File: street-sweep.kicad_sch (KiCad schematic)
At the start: 56 parts, among them J1 PJ-320A, P1 GT-USB-7010ASV, SW10 SW_Push, SW10_r1 SW_Push, SW11 SW_Push, SW11_r1 SW_Push, SW12 SW_Push, SW12_r1 SW_Push, SW13_r1 SW_Push, SW14 SW_Push, SW14_r1 SW_Push, SW15 SW_Push, SW15_r1 SW_Push, SW16 SW_Push, SW16_r1 SW_Push, SW17 SW_Push, SW17_r1 SW_Push, SW18 SW_Push, SW18_r1 SW_Push, SW2 SW_Push, SW20 SW_Push, SW21 SW_Push, SW2_r1 SW_Push, SW3 SW_Push, SW3_r1 SW_Push, SW4 SW_Push, SW4_r1 SW_Push, SW5 SW_Push, SW5_r1 SW_Push, SW6 SW_Push, SW6_r1 SW_Push, SW7_r1 SW_Push, SW8 SW_Push, SW8_r1 SW_Push, SW9 SW_Push, SW9_r1 SW_Push, U1 CH552G

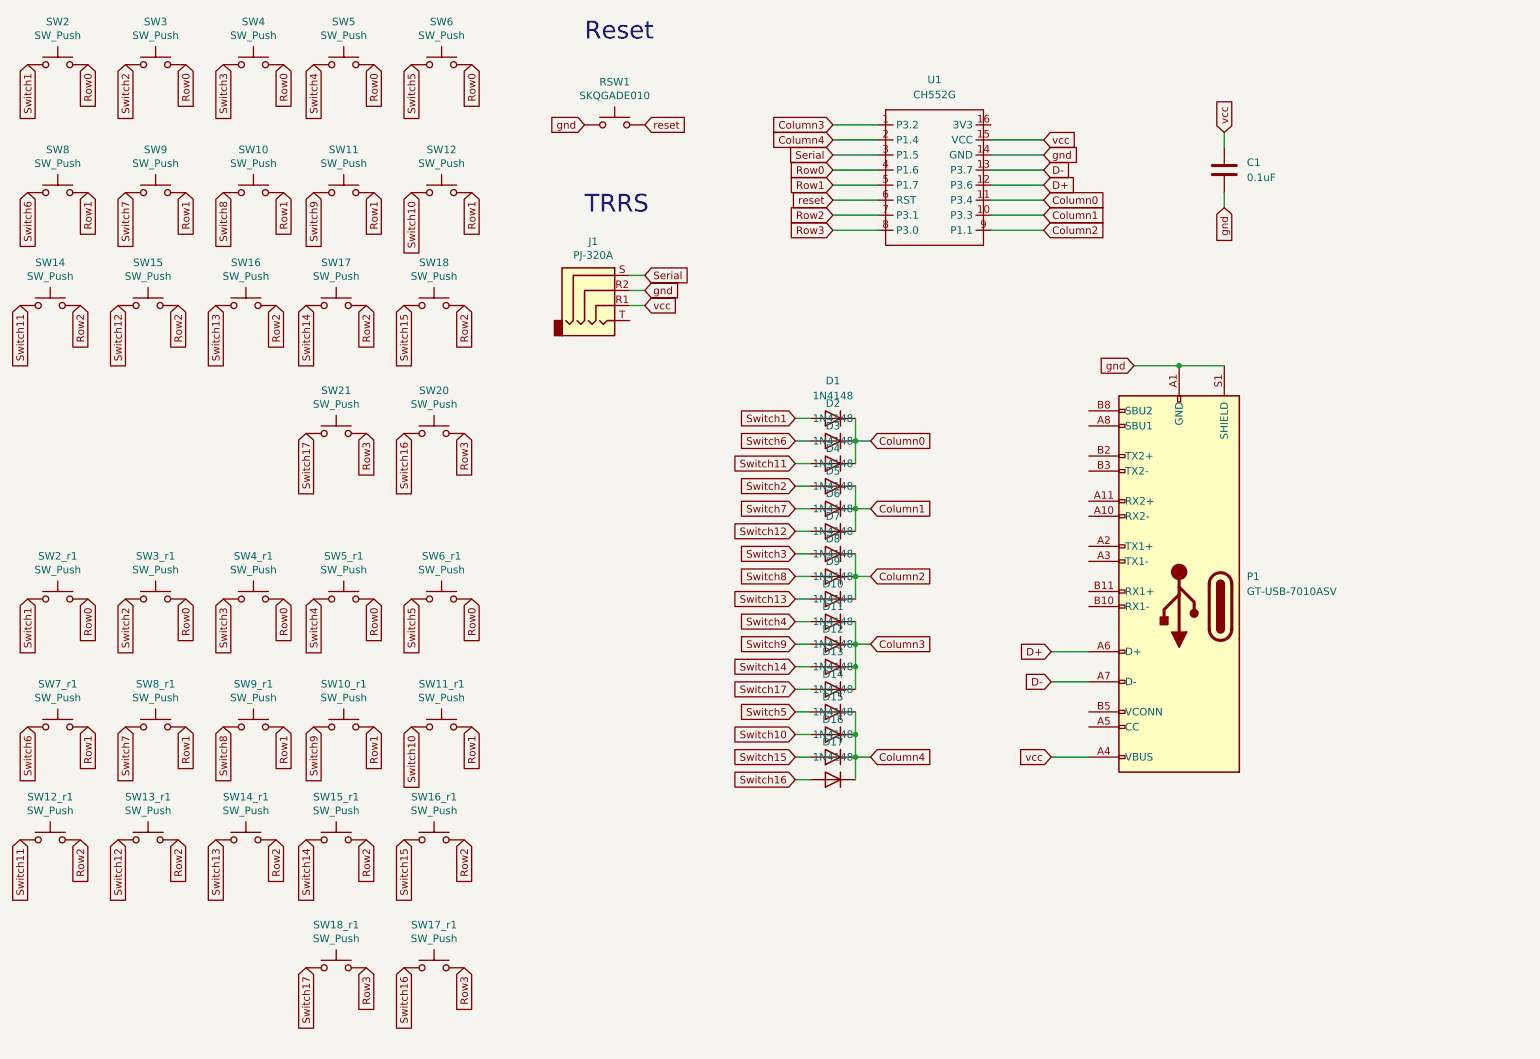
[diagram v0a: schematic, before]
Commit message: Laid out CH552 Board version with two USB-C ports and fixes for flashing.
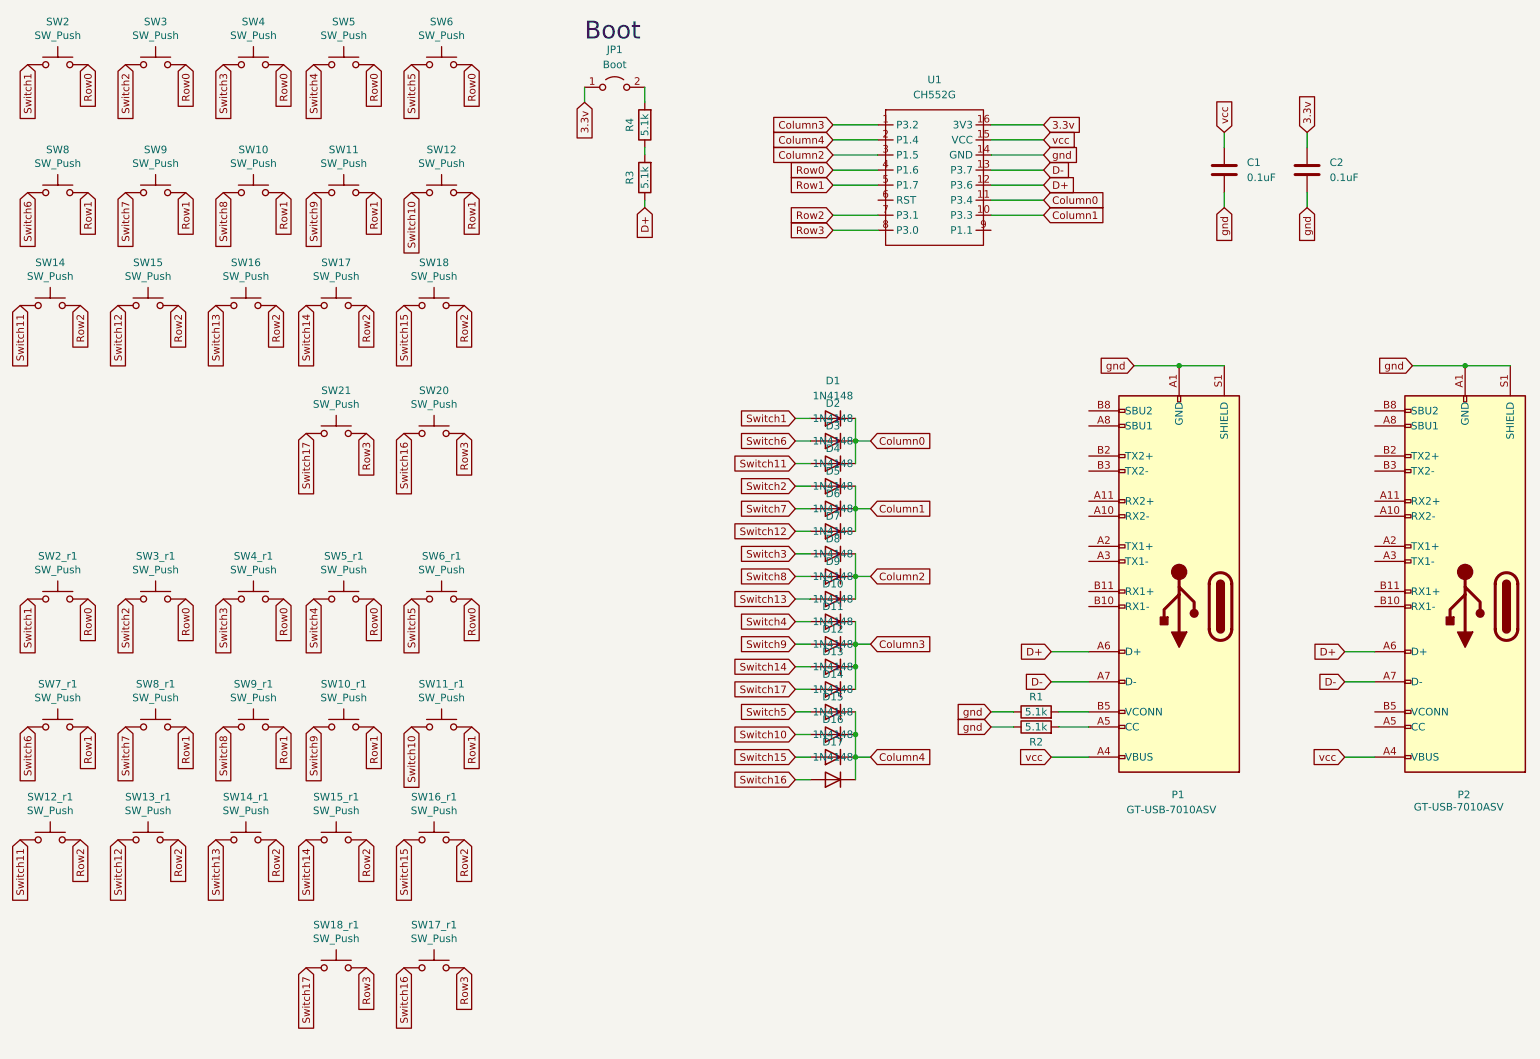
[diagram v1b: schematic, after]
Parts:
- removed J1: PJ-320A, Connector_Audio:Jack_3.5mm_PJ320D_Horizontal, symbol Connector:AudioJack4
- removed RSW1: SKQGADE010, Button_Switch_SMD:SW_SPST_SKQG_WithoutStem, symbol Switch:SW_Push
- added C2: 0.1uF, Capacitor_SMD:C_0805_2012Metric_Pad1.18x1.45mm_HandSolder, symbol Device:C
- added JP1: Boot, Connector_PinHeader_2.54mm:PinHeader_1x02_P2.54mm_Vertical, symbol Jumper:Jumper_2_Open
- added P2: GT-USB-7010ASV, Connector_USB:USB_C_Receptacle_G-Switch_GT-USB-7010ASV, symbol Connector:USB_C_Plug
- added R1, R2, R3, R4: 5.1k, Resistor_SMD:R_0805_2012Metric, symbol Device:R
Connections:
- net Serial is gone; now on net Column2: U1.3 (P1.5)
- net Column2: no longer U1.9 (P1.1)
- net D+: now also P2.A6 (D+), R3.1
- net D-: now also P2.A7 (D-)
- net gnd: now also C2.2, P2.A1 (GND), P2.A12 (GND), P2.B1 (GND), P2.B12 (GND), P2.S1 (SHIELD), R1.1, R2.1
- net vcc: now also P2.A4 (VBUS), P2.A9 (VBUS), P2.B4 (VBUS), P2.B9 (VBUS)
- net 3.3v: now reaches U1.16 (3V3)
- net 3.3v: now also C2.1, JP1.1 (A)
- net at P1.A5 (CC): now also R2.2
- net at P1.B5 (VCONN): now also R1.2
- net reset: no longer names the net of U1.6 (RST)
- new net: JP1.2 (B), R4.2
- new net: R3.2, R4.1
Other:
- note added: "Boot"
- note removed: "Reset"
- note removed: "TRRS"

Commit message: Rotary Encoder added, still on CH552G
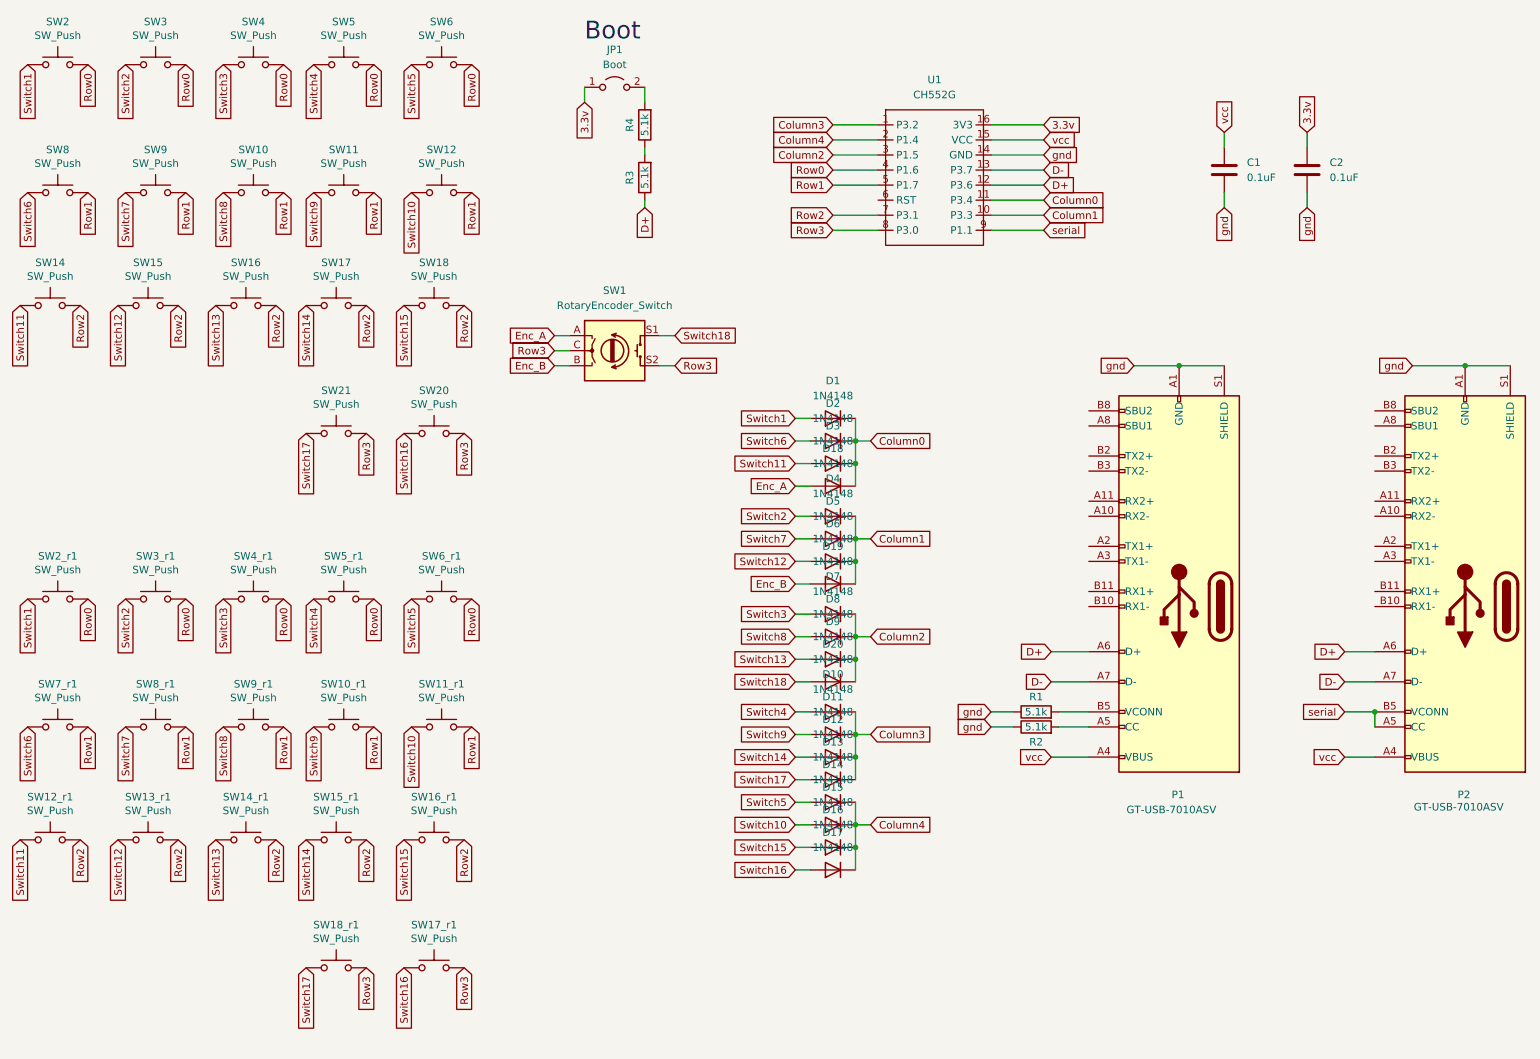
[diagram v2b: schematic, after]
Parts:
- added D18, D19, D20: 1N4148, Diode_SMD:D_SOD-123, symbol Diode:1N4148
- added SW1: RotaryEncoder_Switch, Rotary_Encoder:RotaryEncoder_Alps_EC11E-Switch_Vertical_H20mm, symbol Device:RotaryEncoder_Switch
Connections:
- net Column0: now also D18.1 (K)
- net Column1: now also D19.1 (K)
- net Column2: now also D20.1 (K)
- net Row3: now also SW1.C, SW1.S2
- net serial: now reaches U1.9 (P1.1)
- net serial: now also P2.A5 (CC), P2.B5 (VCONN)
- new net Enc_A: D18.2 (A), SW1.A
- new net Enc_B: D19.2 (A), SW1.B
- new net Switch18: D20.2 (A), SW1.S1
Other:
- moved on the sheet: D10, D11, D12, D13, D14, D15, D16, D17, D4, D5, D6, D7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
